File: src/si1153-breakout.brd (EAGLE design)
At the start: 18 x 9 mm, 9 parts, among them J1 PTH VERT MALE, J2 PTH VERT MALE, U1 SI1153-AB09-GM

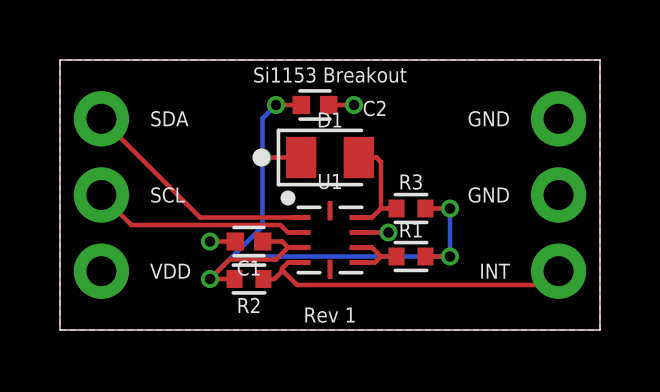
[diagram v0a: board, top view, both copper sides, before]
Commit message: Update to fit OSH Park 2-layer DRU.
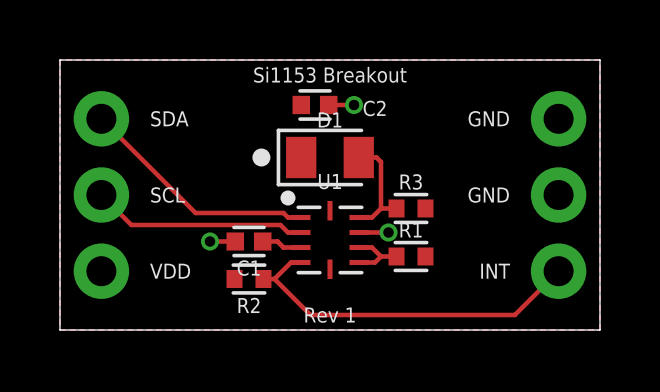
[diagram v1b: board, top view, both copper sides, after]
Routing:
- net VDD: track 24.5 -> 1.35 mm, vias 5 -> 0
- net INT: track 11.1 -> 12.0 mm
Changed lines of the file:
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@@
 <setting verticaltext="up"/>
 </settings>
-<grid distance="1" unitdist="mm" unit="mm" style="lines" multiple="1" display="yes" altdistance="0.1" altunitdist="mm" altunit="mm"/>
+<grid distance="0.1" unitdist="mm" unit="mm" style="lines" multiple="1" display="yes" altdistance="0.05" altunitdist="mm" altunit="mm"/>
 <layers>
 <layer number="1" name="Top" color="4" fill="1" visible="yes" active="yes"/>
@@
 </class>
 </classes>
-<designrules name="stella-wearables">
-<description language="en">&lt;b&gt;Stella Wearables Design Rules based on OSH Park Design Rules&lt;/b&gt;
+<designrules name="oshpark-2layer">
+<description language="en">&lt;b&gt;OSH Park Design Rules&lt;/b&gt;
 &lt;p&gt;
 Please make sure your boards conform to these design rules.
@@
 <param name="mtCopper" value="0.035559375mm 0.0356mm 0.0356mm 0.0356mm 0.0356mm 0.0356mm 0.0356mm 0.0356mm 0.0356mm 0.0356mm 0.0356mm 0.0356mm 0.0356mm 0.0356mm 0.0356mm 0.035559375mm"/>
 <param name="mtIsolate" value="1.6mm 0.1499mm 0.2007mm 0.1499mm 0.2007mm 0.1499mm 0.2007mm 0.1499mm 0.2007mm 0.1499mm 0.2007mm 0.1499mm 0.2007mm 0.1499mm 0.2007mm"/>
-<param name="mdWireWire" value="3mil"/>
-<param name="mdWirePad" value="3mil"/>
-<param name="mdWireVia" value="3mil"/>
-<param name="mdPadPad" value="3mil"/>
-<param name="mdPadVia" value="3mil"/>
-<param name="mdViaVia" value="3mil"/>
-<param name="mdSmdPad" value="3mil"/>
-<param name="mdSmdVia" value="3mil"/>
-<param name="mdSmdSmd" value="3mil"/>
+<param name="mdWireWire" value="6mil"/>
+<param name="mdWirePad" value="6mil"/>
+<param name="mdWireVia" value="6mil"/>
+<param name="mdPadPad" value="6mil"/>
+<param name="mdPadVia" value="6mil"/>
+<param name="mdViaVia" value="6mil"/>
+<param name="mdSmdPad" value="6mil"/>
+<param name="mdSmdVia" value="6mil"/>
+<param name="mdSmdSmd" value="6mil"/>
 <param name="mdViaViaSameLayer" value="8mil"/>
 <param name="mnLayersViaInSmd" value="2"/>
@@
 <param name="mdDrill" value="6mil"/>
 <param name="mdSmdStop" value="0mil"/>
-<param name="msWidth" value="3mil"/>
-<param name="msDrill" value="6mil"/>
+<param name="msWidth" value="6mil"/>
+<param name="msDrill" value="10mil"/>
 <param name="msMicroVia" value="10mil"/>
 <param name="msBlindViaRatio" value="0.5"/>
@@
 <contactref element="J1" pad="1"/>
 <contactref element="U1" pad="1"/>
-<wire x1="-7.62" y1="2.54" x2="-4.33" y2="-0.75" width="0.1524" layer="1"/>
-<wire x1="-4.33" y1="-0.75" x2="-0.975" y2="-0.75" width="0.1524" layer="1"/>
+<wire x1="-0.975" y1="-0.75" x2="-1.4" y2="-0.75" width="0.1524" layer="1"/>
+<wire x1="-1.4" y1="-0.75" x2="-1.55" y2="-0.6" width="0.1524" layer="1"/>
+<wire x1="-1.55" y1="-0.6" x2="-4.48" y2="-0.6" width="0.1524" layer="1"/>
+<wire x1="-4.48" y1="-0.6" x2="-7.62" y2="2.54" width="0.1524" layer="1"/>
 </signal>
 <signal name="VDD">
@@
 <contactref element="D1" pad="A"/>
 <contactref element="C2" pad="1"/>
-<wire x1="-0.975" y1="-1.75" x2="-1.4" y2="-1.75" width="0.1524" layer="1"/>
-<via x="-4" y="-2.8" extent="1-16" drill="0.35" diameter="0.1524"/>
-<wire x1="-3.1825" y1="-2.8" x2="-4" y2="-2.8" width="0.1524" layer="1"/>
-<wire x1="-3.35" y1="-2.15" x2="-4" y2="-2.8" width="0.1524" layer="1"/>
-<wire x1="-1.4" y1="-1.75" x2="-1.8" y2="-2.15" width="0.1524" layer="1"/>
-<wire x1="-1.8" y1="-2.15" x2="-3.35" y2="-2.15" width="0.1524" layer="1"/>
-<via x="4" y="-0.45" extent="1-16" drill="0.35" diameter="0.1524"/>
-<via x="4" y="-2.05" extent="1-16" drill="0.35" diameter="0.1524"/>
-<wire x1="4" y1="-2.05" x2="3.1825" y2="-2.05" width="0.1524" layer="1"/>
-<wire x1="3.1825" y1="-0.45" x2="4" y2="-0.45" width="0.1524" layer="1"/>
-<wire x1="-2.2425" y1="-1.55" x2="-1.6" y2="-1.55" width="0.1524" layer="1"/>
-<wire x1="-1.6" y1="-1.55" x2="-1.4" y2="-1.75" width="0.1524" layer="1"/>
-<via x="-2.25" y="1.25" extent="1-16" drill="0.35" diameter="0.1524"/>
-<wire x1="-0.9596" y1="1.25" x2="-2.25" y2="1.25" width="0.1524" layer="1"/>
-<via x="-1.8" y="3" extent="1-16" drill="0.35" diameter="0.1524"/>
-<wire x1="-0.9575" y1="3" x2="-1.8" y2="3" width="0.1524" layer="1"/>
-<wire x1="-1.8" y1="3" x2="-2.25" y2="2.55" width="0.1524" layer="16"/>
-<wire x1="-2.25" y1="2.55" x2="-2.25" y2="1.25" width="0.1524" layer="16"/>
-<wire x1="-2.25" y1="1.25" x2="-2.25" y2="-1.05" width="0.1524" layer="16"/>
-<wire x1="-2.25" y1="-1.05" x2="-3.25" y2="-2.05" width="0.1524" layer="16"/>
-<wire x1="-3.25" y1="-2.05" x2="-4" y2="-2.8" width="0.1524" layer="16"/>
-<wire x1="4" y1="-2.05" x2="-3.25" y2="-2.05" width="0.1524" layer="16"/>
-<wire x1="4" y1="-2.05" x2="4" y2="-0.45" width="0.1524" layer="16"/>
 <polygon width="0.1524" layer="1">
 <vertex x="-9" y="-4.5"/>
@@
 <vertex x="-9" y="4.5"/>
 </polygon>
+<wire x1="-0.975" y1="-1.75" x2="-1.55" y2="-1.75" width="0.1524" layer="1"/>
+<wire x1="-1.75" y1="-1.55" x2="-2.2425" y2="-1.55" width="0.1524" layer="1"/>
+<wire x1="-1.55" y1="-1.75" x2="-1.75" y2="-1.55" width="0.1524" layer="1"/>
 </signal>
 <signal name="INT">
@@
 <contactref element="U1" pad="4"/>
 <contactref element="R2" pad="1"/>
-<wire x1="-0.975" y1="-2.25" x2="-1.4" y2="-2.25" width="0.1524" layer="1"/>
-<wire x1="-1.4" y1="-2.25" x2="-1.6" y2="-2.45" width="0.1524" layer="1"/>
-<wire x1="-1.6" y1="-2.45" x2="-1.6" y2="-2.5" width="0.1524" layer="1"/>
-<wire x1="-1.6" y1="-2.5" x2="-1.6" y2="-2.55" width="0.1524" layer="1"/>
+<wire x1="-0.975" y1="-2.25" x2="-1.3" y2="-2.25" width="0.1524" layer="1"/>
+<wire x1="-1.3" y1="-2.25" x2="-1.85" y2="-2.8" width="0.1524" layer="1"/>
 <wire x1="-2.2175" y1="-2.8" x2="-1.85" y2="-2.8" width="0.1524" layer="1"/>
-<wire x1="-1.85" y1="-2.8" x2="-1.6" y2="-2.55" width="0.1524" layer="1"/>
-<wire x1="-1.6" y1="-2.5" x2="-1.1" y2="-3" width="0.1524" layer="1"/>
-<wire x1="7.16" y1="-3" x2="7.62" y2="-2.54" width="0.1524" layer="1"/>
-<wire x1="-1.1" y1="-3" x2="7.16" y2="-3" width="0.1524" layer="1"/>
+<wire x1="-1.85" y1="-2.8" x2="-0.65" y2="-4" width="0.1524" layer="1"/>
+<wire x1="6.16" y1="-4" x2="7.62" y2="-2.54" width="0.1524" layer="1"/>
+<wire x1="-0.65" y1="-4" x2="6.16" y2="-4" width="0.1524" layer="1"/>
 </signal>
 <signal name="N$1">
